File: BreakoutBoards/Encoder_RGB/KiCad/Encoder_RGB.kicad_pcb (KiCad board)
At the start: 2 copper layers, 3 parts, among them J1 Conn_01x06_Pin

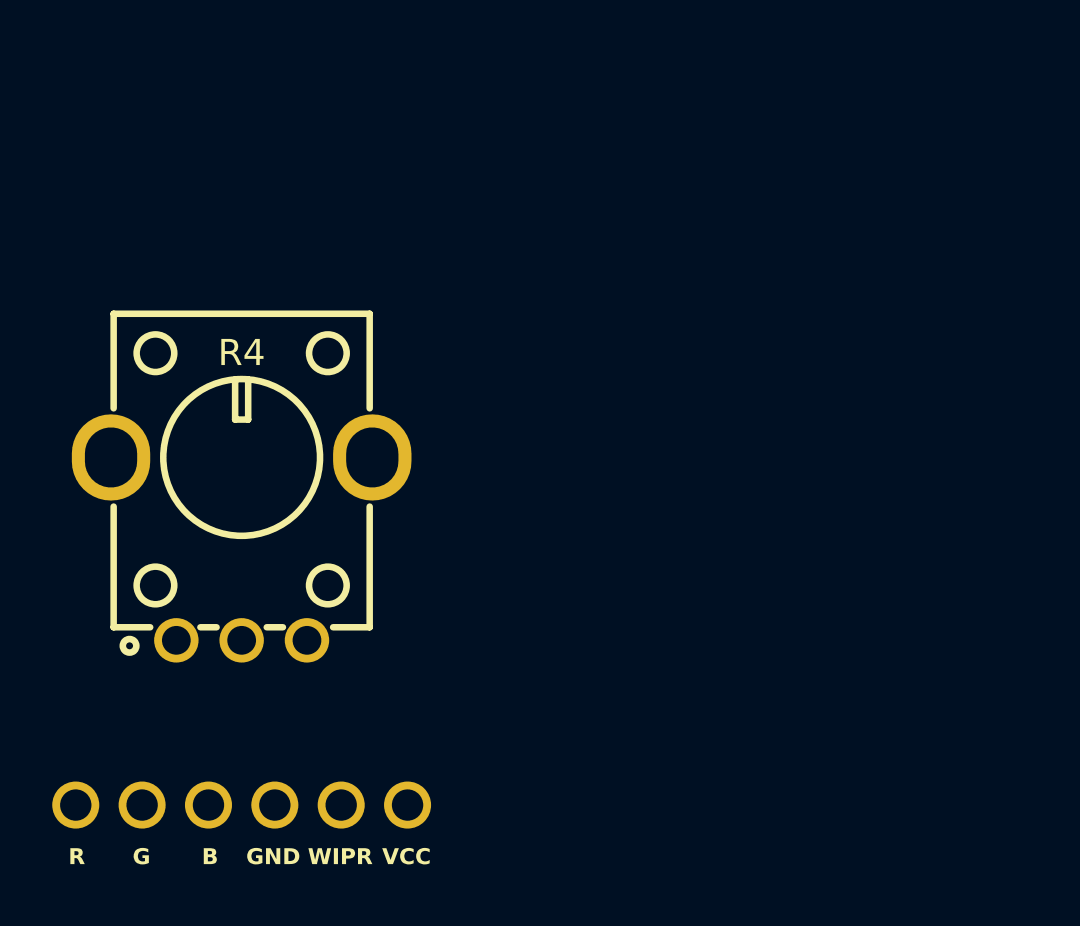
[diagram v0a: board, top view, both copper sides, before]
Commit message: removing resistors to make more versatile and selecting new led to use
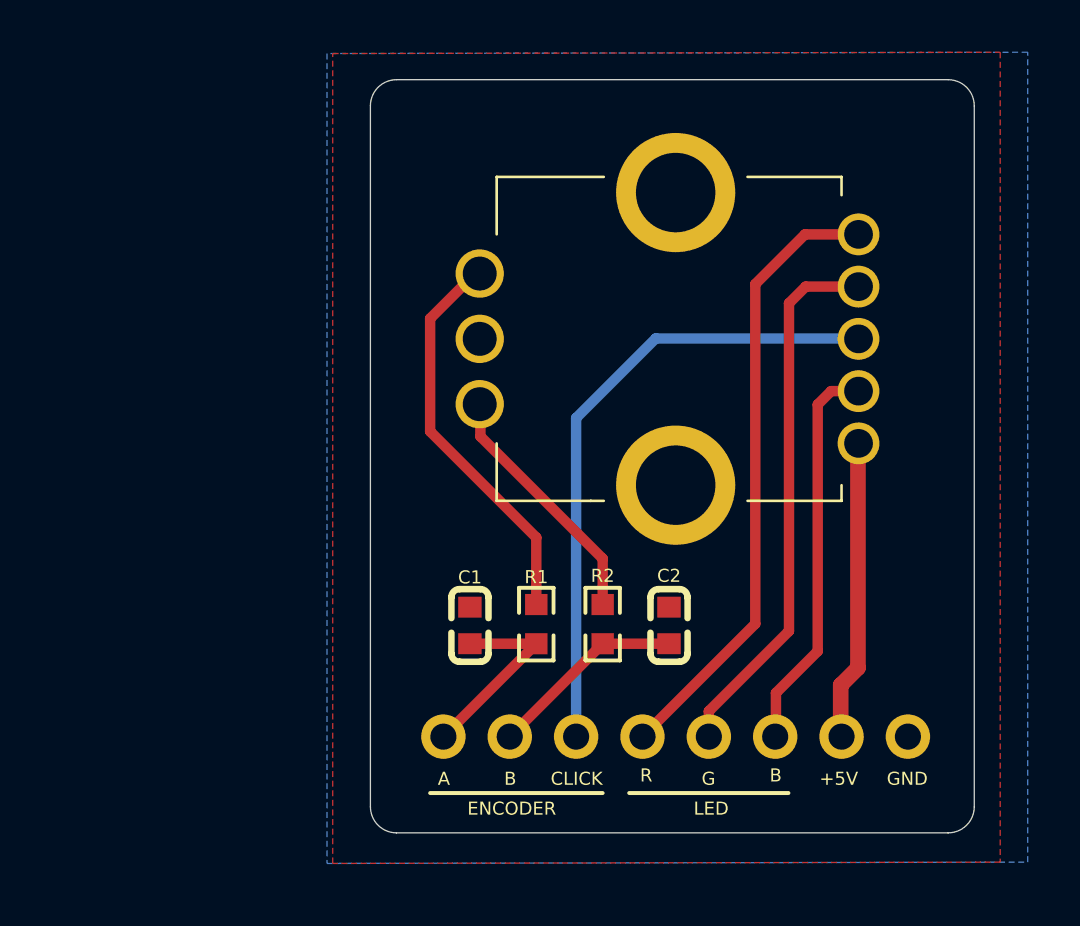
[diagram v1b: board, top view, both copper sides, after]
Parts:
- removed R4: RK09K1130D62, clectric-diy:RES-TH_RK09K113004U
- added C1: 10nF, clectric-diy:C0603, F.Cu at (99.5, 94.7)
- added C2: 10nF, clectric-diy:C0603, F.Cu at (107.1, 94.7)
- added R1: 10K, clectric-diy:R0603, F.Cu at (102.0, 94.7)
- added R2: 10K, clectric-diy:R0603, F.Cu at (104.6, 94.7)
- added S1: PEL12T-4225S-S1024, clectric-diy:PEL12T4225SS1024, F.Cu at (107.1, 83.8)
- J1: value Conn_01x06_Pin -> Conn_01x08_Pin; footprint clectric-diy:HDR-TH_6P-P2.54-V-M-1 -> Connector_PinHeader_2.54mm:PinHeader_1x08_P2.54mm_Vertical
- moved G*** 16.2 mm to (107.1, 83.8)
- moved J1 8.15 mm to (98.5, 99.0), turned to -90 degrees
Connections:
- J1 pad 1: LED_RED -> ENC_A
- J1 pad 2: LED_GREEN -> ENC_B
- J1 pad 3: LED_BLUE -> ENC_CLICK
- J1 pad 4: GND+CCW -> LED_RED
- J1 pad 5: WIPER -> LED_GREEN
- J1 pad 6: VCC+CW -> LED_BLUE
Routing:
- net ENC_CLICK: track 0.00 -> 24.3 mm
- net LED_RED: track 0.00 -> 23.9 mm
- net ENC_A: track 0.00 -> 22.8 mm
- net LED_GREEN: track 0.00 -> 20.8 mm
- net ENC_B: track 0.00 -> 17.2 mm
- net LED_BLUE: track 0.00 -> 15.2 mm
- net +5V: track 0.00 -> 11.5 mm
- added copper zone on B.Cu, net GND
- added copper zone on F.Cu, net GND
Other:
- board outline added: 23.1 x 28.8 mm
- board text added: "+5V"
- board text added: "A"
- board text added: "CLICK"
- board text added: "Charge Encoder_RGB Mk 0.1"
- board text added: "ENCODER"
- board text added: "Encoder PEL12T4225SS1024 Resistors FRC0603F1002TS Capacitors FCC0603B103K500CT"
- board text added: "LED"
- board text removed: "Charge Potentiometer_RGB Mk 0.1"
- board text removed: "LED E6C1206RGBC3UDA Potentiometer RK09K1130D62"
- board text removed: "VCC"
- board text removed: "WIPR"

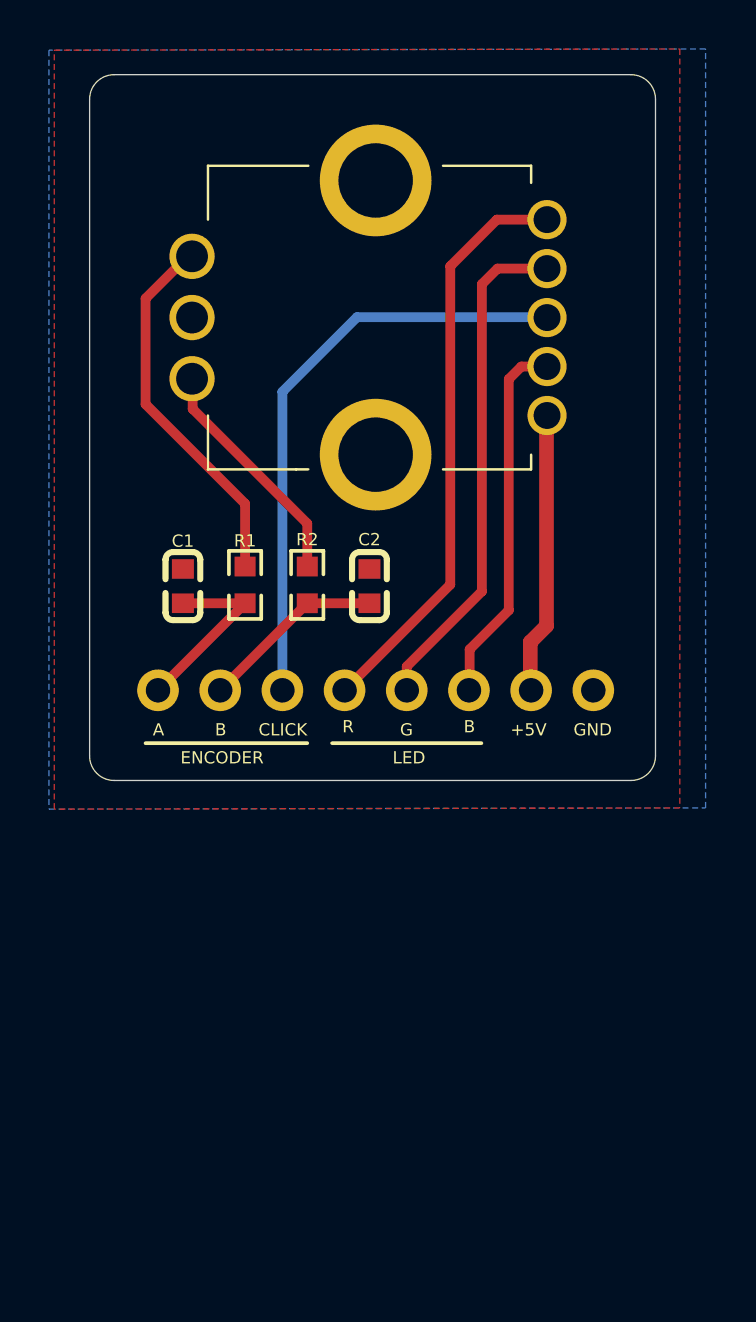
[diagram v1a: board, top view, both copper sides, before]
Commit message: updated to Mk1 and sent for manufacturing
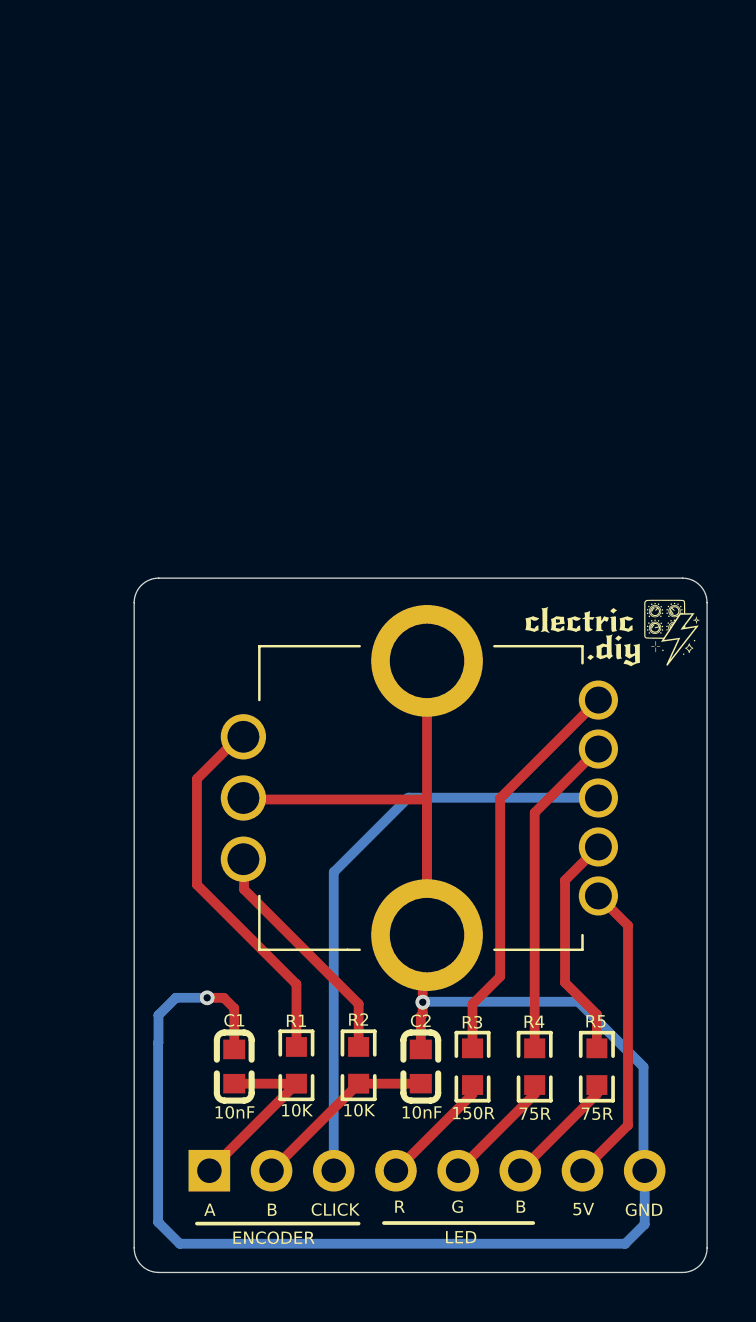
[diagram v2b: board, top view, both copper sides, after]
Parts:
- removed the G*** at (107.1, 83.8)
- added G***: LOGO, clectric-diy-branding:clectric.diy-Wordmark-7.5mm, F.Cu at (117.0, 96.6)
- added G***: LOGO, clectric-diy-branding:clectric.diy-Wordmark-7.5mm, B.Cu at (102.8, 97.3)
- added R3: 150R, clectric-diy:R0603, F.Cu at (111.3, 114.4)
- added R4: 75R, clectric-diy:R0603, F.Cu at (113.9, 114.4)
- added R5: 75R, clectric-diy:R0603, F.Cu at (116.4, 114.4)
- moved C1 19.7 mm to (101.6, 114.3)
- moved C2 19.7 mm to (109.2, 114.3)
- moved J1 19.7 mm to (100.6, 118.6)
- moved R1 19.7 mm to (104.1, 114.3)
- moved R2 19.7 mm to (106.7, 114.3)
- moved S1 19.7 mm to (109.2, 103.4)
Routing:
- net GND: track 0.00 -> 79.9 mm, vias 0 -> 2
- net LED_RED: track 23.9 -> 21.2 mm
- net LED_GREEN: track 20.8 -> 18.1 mm
- net +5V: track 11.5 -> 12.6 mm
- net LED_BLUE: track 15.2 -> 14.2 mm
- removed copper zone on B.Cu, net GND
- removed copper zone on F.Cu, net GND
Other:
- board size 23.1 x 28.8 mm -> 23.4 x 28.4 mm
- board text added: "5V"
- board text added: "Charge Encoder w/ RGB LED Mk1"
- board text added: "Encoder: PEL12T4225SS1024"
- board text removed: "+5V"
- board text removed: "Charge Encoder_RGB Mk 0.1"
- board text removed: "Encoder PEL12T4225SS1024 Resistors FRC0603F1002TS Capacitors FCC0603B103K500CT"

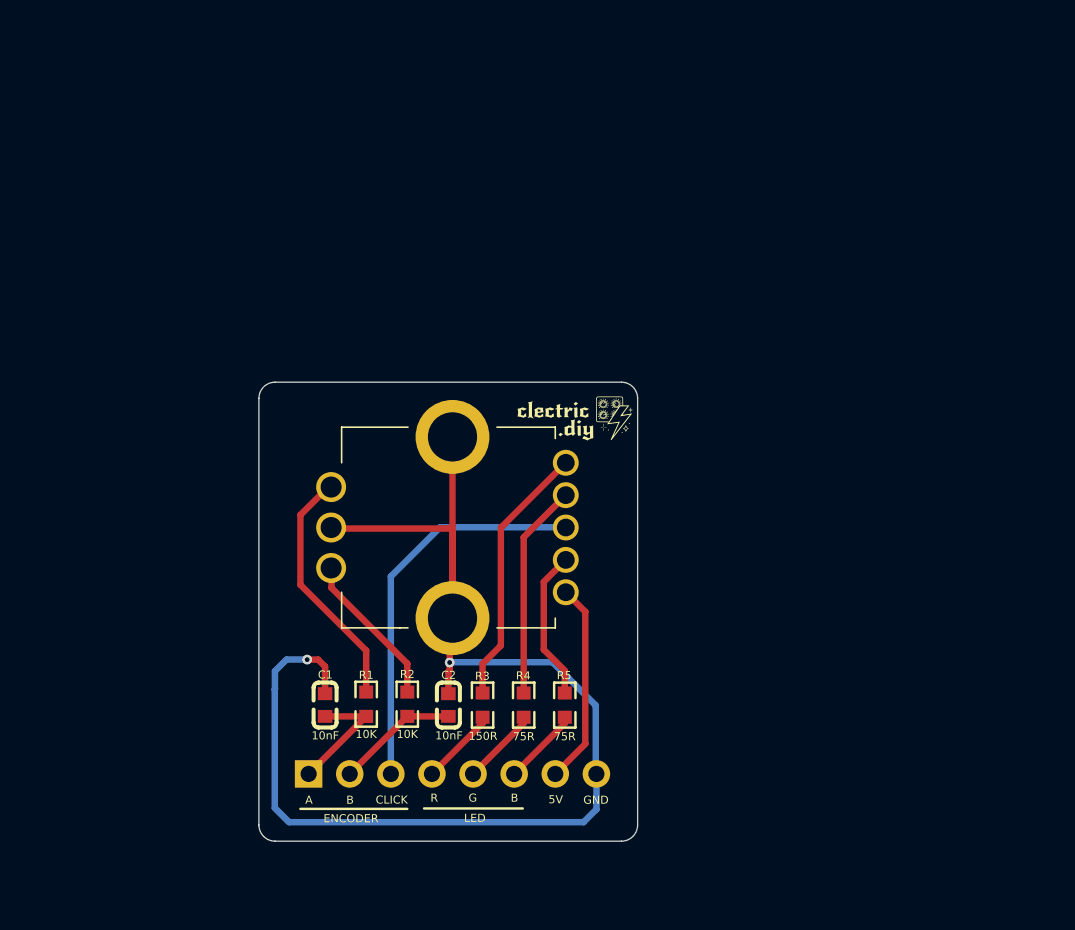
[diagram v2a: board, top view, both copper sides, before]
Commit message: renaming and reorganizing to clarify use
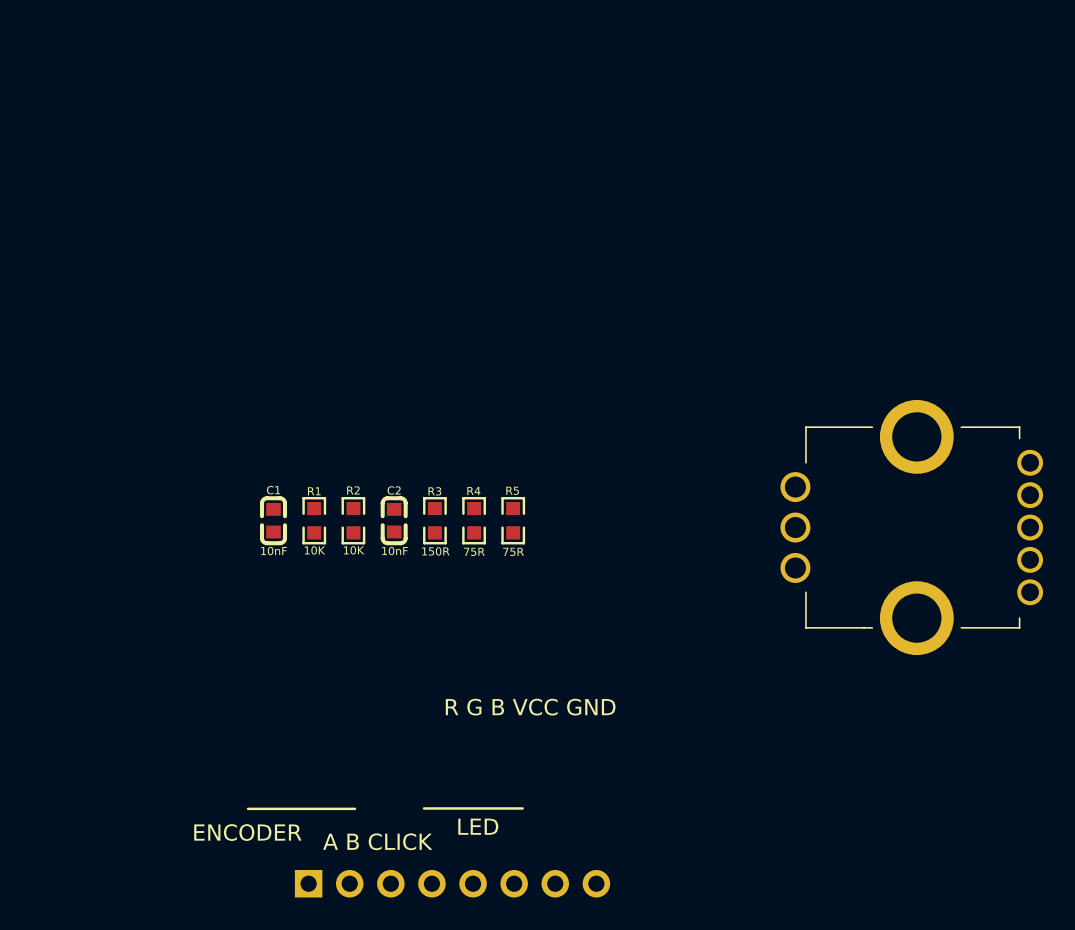
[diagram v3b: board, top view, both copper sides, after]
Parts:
- removed G*** (x2): LOGO, clectric-diy-branding:clectric.diy-Wordmark-7.5mm
- moved S1 28.7 mm to (137.9, 103.4)
- moved C2 11.9 mm to (105.9, 103.0)
- moved R5 11.8 mm to (113.2, 103.0)
- moved C1 11.8 mm to (98.4, 103.0)
- moved R2 11.8 mm to (103.3, 103.0)
- moved R4 11.8 mm to (110.8, 103.0)
- moved R1 11.8 mm to (100.9, 103.0)
- moved R3 11.8 mm to (108.4, 103.0)
- moved J1 6.78 mm to (100.6, 125.4)
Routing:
- net GND: track 79.9 -> 0.00 mm, vias 2 -> 0
- net ENC_CLICK: track 24.3 -> 0.00 mm
- net ENC_A: track 22.8 -> 0.00 mm
- net LED_RED: track 21.2 -> 0.00 mm
- net LED_GREEN: track 18.1 -> 0.00 mm
- net ENC_B: track 17.2 -> 0.00 mm
- net LED_BLUE: track 14.2 -> 0.00 mm
- net +5V: track 12.6 -> 0.00 mm
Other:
- board outline removed
- board text added: "A B CLICK"
- board text added: "Charge Encoder w/ RGB LED Mk1.1"
- board text added: "R G B VCC GND"
- board text removed: "5V"
- board text removed: "A"
- board text removed: "B"
- board text removed: "CLICK"
- board text removed: "Charge Encoder w/ RGB LED Mk1"
- board text removed: "G"
- board text removed: "GND"
- board text removed: "R"
